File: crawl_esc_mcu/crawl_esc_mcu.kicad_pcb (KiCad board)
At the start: 2 copper layers, 28 x 32 mm, 43 parts, among them IC1 LP2981-33DBVTE4, IC2 STM32F051K8U7_MY, IC3 FD6288Q

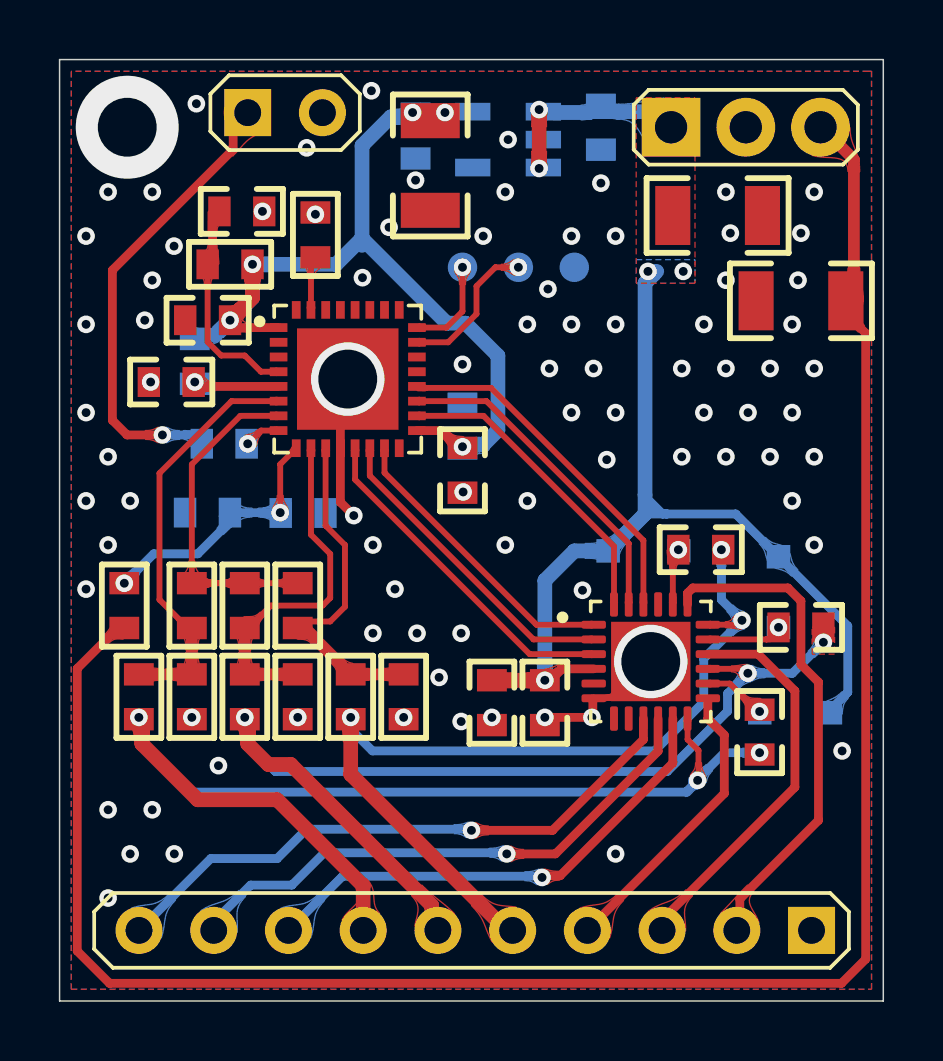
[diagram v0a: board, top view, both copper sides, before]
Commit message: change stepup isens layout
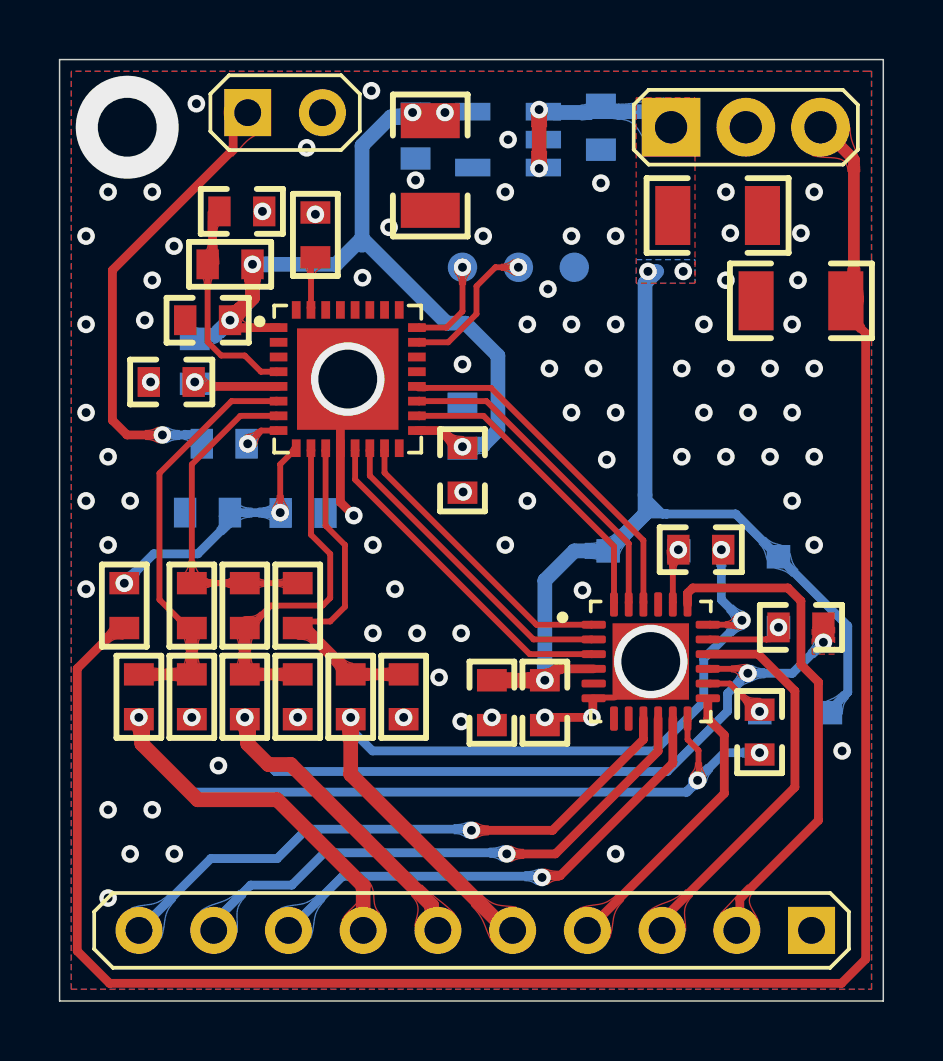
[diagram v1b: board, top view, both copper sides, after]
